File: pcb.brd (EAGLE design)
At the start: 88.9 x 70 mm, 70 parts, among them U1 MSP430F5172, U10 DCH010505S_EDJ_4, U11 ISO7420_D_8, U12 TS5A3357_DCU_8, U13 TS5A3357_DCU_8, U14 TLV2242_D_8, U2 ISO7221A_D_8, U3 MAX232E_D_16, U4 ISO7221A_D_8, U5 DCH010505S_EDJ_4, U6 REG101-3_DBV_5, U7 DCH010505S_EDJ_4, U8 TCA6416A_PW_24

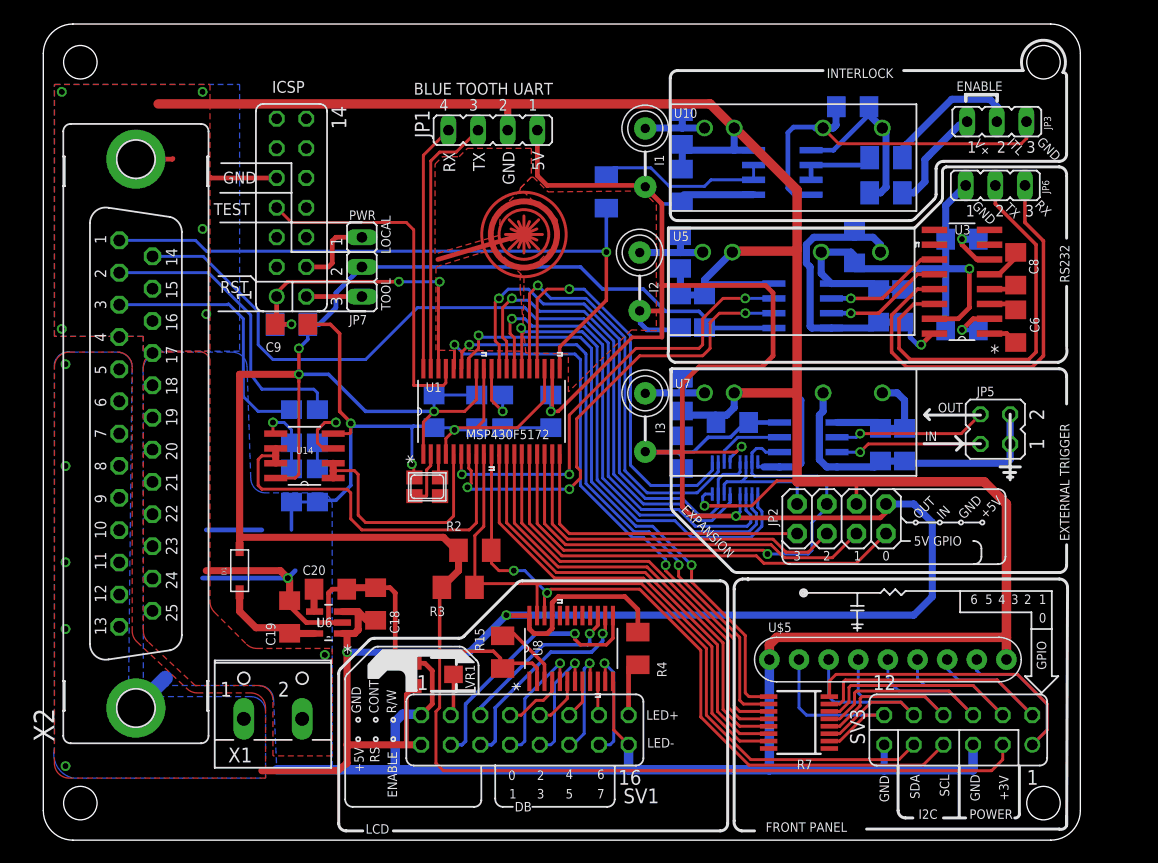
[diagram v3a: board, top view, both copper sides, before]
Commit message: Extensive Silkscreen update, LEDS
Added power, rx and tx LEDs
Updates silk screen documentation
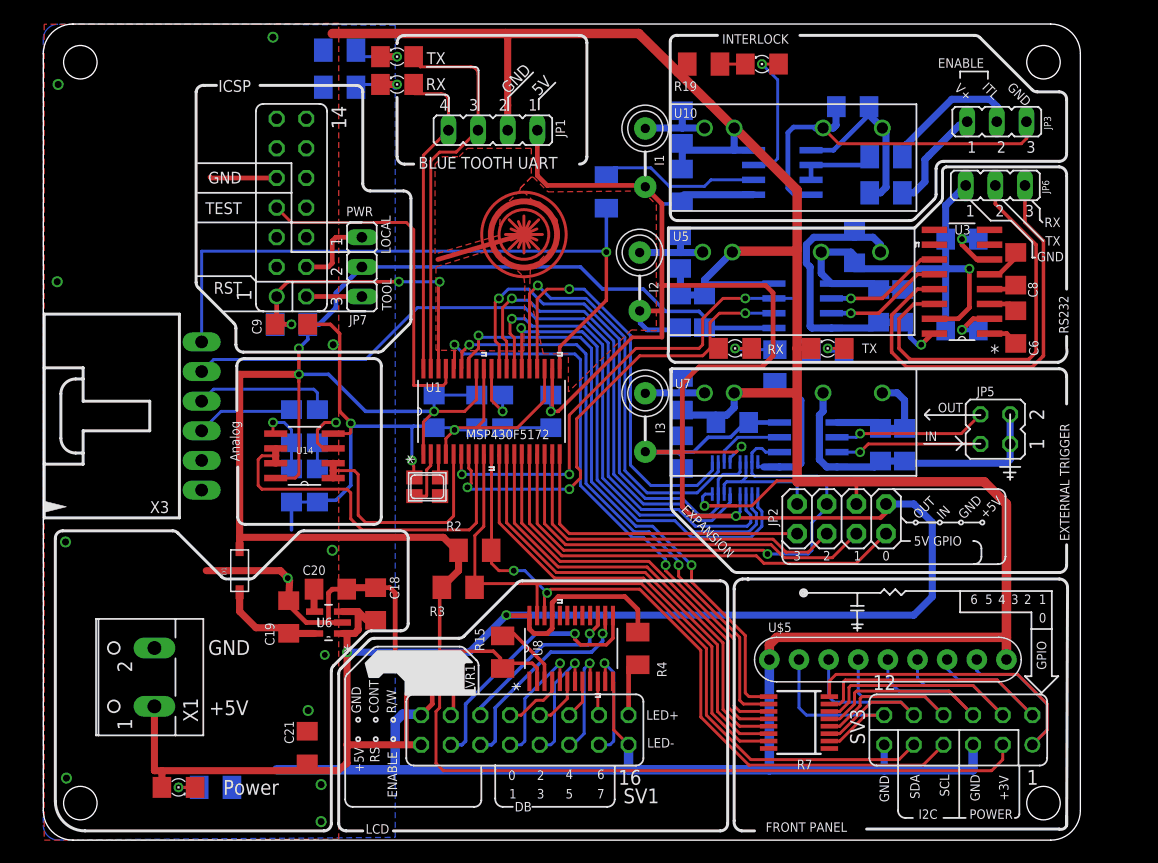
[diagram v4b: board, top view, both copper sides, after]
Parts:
- removed X2: (no value), con-subd:F25VP
- added C21: 10 uF, adafruit:C1206
- added LED1, LED2, LED3, LED4, LED5, LED6: (no value), led:1206
- added R12: 47k, adafruit:M1206
- added R13, R16, R17, R18, R19: 100k, adafruit:M1206
- added X3: C-GRID-06-70553, con-molex:70553-06
- R11: value 750k -> 100k
- U11: value ISO7420_D_8 -> ISO7420Fx
- moved X1 11.7 mm to (8.26, 14.0), turned to 90 degrees
- moved C16 0.08 mm to (54.8, 38.3)
- moved C19 0.08 mm to (21.0, 19.1)
- moved C29 0.08 mm to (54.8, 61.1)
- moved C6 0.08 mm to (83.3, 44.0)
- moved R5 0.08 mm to (72.2, 58.6)
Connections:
- new net N$25: LED1.C, R12.2
- new net N$26: LED2.C, R13.2
- new net N$29: LED3.C, R16.2
- new net N$30: LED6.C, R19.2
- new net N$31: LED5.C, R17.1
- new net N$32: LED6.A, U11.7
- new net N$33: LED4.A, R18.2
- net GND: now also C21.2, LED4.C, R12.1, R13.1, R16.1, R17.2, R19.1, X3.1, X3.2; no longer X2.17, X2.18, X2.19, X2.20, X2.21, X2.22, X2.23, X2.24, X2.25, X2.G1, X2.G2
- net LASER_CURRENT: now also X3.4; no longer X2.2
- net LASER_ILK: now also X3.6; no longer X2.1
- net LASER_ILK_HIGH: no longer U11.7
- net LASER_TEMPERATURE: now also X3.3; no longer X2.3
- net LASER_TTL: now also X3.5; no longer X2.14
- net RX1: now also LED5.A
- net RX2: now also LED3.A
- net TX1: now also R18.1
- net TX2: now also LED2.A
- net VCC_5V: now also C21.1, LED1.A; no longer X2.10, X2.11, X2.12, X2.13, X2.5, X2.6, X2.7, X2.8, X2.9
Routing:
- net GND: track 431.2 -> 408.3 mm, vias 11 -> 16
- net VCC_5V: track 258.9 -> 275.7 mm, vias 10 -> 5
- net LASER_TEMPERATURE: track 22.6 -> 8.45 mm
- net LASER_CURRENT: track 25.8 -> 11.9 mm
- net N$32: track 0.00 -> 12.4 mm, vias 0 -> 1
- net TX2: track 23.0 -> 34.4 mm
- net LASER_TTL: track 75.7 -> 66.5 mm
- net TX1: track 39.0 -> 45.9 mm
- net RX2: track 21.3 -> 27.9 mm
- net N$29: track 0.00 -> 5.95 mm, vias 0 -> 1
- net N$26: track 0.00 -> 5.50 mm, vias 0 -> 1
- net N$31: track 0.00 -> 4.88 mm, vias 0 -> 1
- net N$25: track 0.00 -> 3.20 mm, vias 0 -> 1
- net N$33: track 0.00 -> 2.92 mm, vias 0 -> 1
- net N$30: track 0.00 -> 2.18 mm
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- removed copper zone on layer 1, net VCC_5V
- removed copper zone on layer 16, net VCC_5V
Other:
- board text added: "Analog"
- board text added: "Current"
- board text added: "Interlock"
- board text added: "MCU"
- board text added: "Power"
- board text added: "Temperature"
- board text added: "Trigger"

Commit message: Silk updates
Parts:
- renumbered C1 to C8.5, C10 to C8.10, C11 to C8.9, C12 to C8.3, C13 to C8.2, C14 to C8.1, C15 to C6.3, C16 to C6.2, C17 to C6.1, C18 to C1.2, C19 to C1.4, C2 to C9.3, C20 to C1.3, C21 to C1.1, C29 to C9.2, C3 to C6.5, C30 to C9.1, C31 to C5.1, C32 to C5.2, C33 to C5.4, C34 to C5.3, C4 to C6.4, C5 to C8.4, C6 to C8.6, C7 to C8.8, C8 to C8.7, C9 to C7.1, I1 to L9.1, I2 to L8.1, I3 to L6.1, JP1 to H8.2, JP2 to H6.1, JP3 to H9.1, JP5 to H6.2, JP6 to H8.1, JP7 to H7.1, LED2 to LED8.3, LED3 to LED8.4, LED4 to LED8.1, LED5 to LED8.2, LED6 to LED9.1, Q2 to XTL, R1 to R4.1, R10 to R7.1, R11 to R9.1, R12 to R1.1, R13 to R8.3, R14 to R9.2, R15 to R2.1, R16 to R8.4, R17 to R8.2, R18 to R8.1, R19 to R9.4, R2 to R5.1, R3 to R5.2, R4 to R2.2, R5 to R9.3, R6 to R4.2, R7 to R3.1, R8 to R4.3, R9 to R4.4, SV1 to H2.1, SV3 to H3.1, U$5 to C3.1, U1 to MCU, U10 to U9.1, U11 to U9.2, U12 to U6.3, U13 to U6.4, U14 to U4.1, U2 to U6.2, U3 to U8.2, U4 to U8.3, U5 to U8.1, U6 to U1.1, U7 to U6.1, U8 to U2.1, X1 to EXT_POWER, X3 to LASER_COM
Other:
- board text added: "1.0"
- board text added: "1.1"
- board text added: "1.2"
- board text added: "1.3"
- board text added: "1.6"
- board text added: "2.0"
- board text added: "2.1"
- board text added: "2.2"
- board text added: "2013 Matthew Beals"
- board text added: "3.1"
- board text added: "3.2"
- board text added: "github.com/mjbeals/Laser_controller"

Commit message: Silk screen updates
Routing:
- net N$23: track 7.61 -> 0.00 mm
- removed copper zone on layer 1, net N$16
- removed copper zone on layer 1, net N$20
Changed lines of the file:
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@@
 <wire x1="1.031875" y1="3.33375" x2="1.031875" y2="25.87625" width="0.254" layer="121"/>
 <wire x1="1.031875" y1="25.87625" x2="1.666875" y2="26.51125" width="0.254" layer="121" curve="-90"/>
-<wire x1="30.63875" y1="26.51125" x2="31.27375" y2="25.87625" width="0.254" layer="121" curve="-90"/>
-<wire x1="31.27375" y1="25.87625" x2="31.27375" y2="18.57375" width="0.254" layer="121"/>
 <wire x1="31.27375" y1="18.57375" x2="30.63875" y2="17.93875" width="0.254" layer="121" curve="-90"/>
 <wire x1="30.63875" y1="17.93875" x2="28.12365" y2="17.93875" width="0.254" layer="121"/>
@@
 <wire x1="11.5366125" y1="26.3252625" x2="15.2921375" y2="22.5697375" width="0.254" layer="121"/>
 <wire x1="15.2921375" y1="22.5697375" x2="15.74115" y2="22.38375" width="0.254" layer="121" curve="45"/>
-<wire x1="30.559375" y1="26.51125" x2="22.329275" y2="26.51125" width="0.254" layer="121"/>
+<wire x1="31.0877625" y1="24.4747375" x2="29.2372375" y2="26.3252625" width="0.254" layer="121"/>
+<wire x1="29.2372375" y1="26.3252625" x2="28.788225" y2="26.51125" width="0.254" layer="121" curve="45"/>
+<wire x1="28.788225" y1="26.51125" x2="22.329275" y2="26.51125" width="0.254" layer="121"/>
 <wire x1="22.329275" y1="26.51125" x2="21.8802625" y2="26.3252625" width="0.254" layer="121" curve="45"/>
 <wire x1="21.8802625" y1="26.3252625" x2="18.1247375" y2="22.5697375" width="0.254" layer="121"/>
@@
 <wire x1="30.32125" y1="68.341875" x2="30.95625" y2="68.976875" width="0.254" layer="121" curve="-90"/>
 <wire x1="45.958125" y1="68.976875" x2="46.593125" y2="68.341875" width="0.254" layer="121" curve="-90"/>
-<wire x1="46.593125" y1="68.341875" x2="46.593125" y2="57.62625" width="0.254" layer="121"/>
-<wire x1="46.593125" y1="57.62625" x2="45.958125" y2="56.99125" width="0.254" layer="121" curve="-90"/>
-<wire x1="45.958125" y1="56.99125" x2="30.95625" y2="56.99125" width="0.254" layer="121"/>
+<wire x1="46.593125" y1="68.341875" x2="46.593125" y2="56.1975" width="0.254" layer="121"/>
+<wire x1="46.593125" y1="56.1975" x2="46.19625" y2="55.800625" width="0.254" layer="121" curve="-90"/>
+<wire x1="33.9725" y1="55.800625" x2="33.416875" y2="56.35625" width="0.254" layer="121" curve="-90"/>
+<wire x1="33.416875" y1="56.35625" x2="32.781875" y2="56.99125" width="0.254" layer="121" curve="90"/>
+<wire x1="32.781875" y1="56.99125" x2="30.95625" y2="56.99125" width="0.254" layer="121"/>
 <wire x1="30.32125" y1="63.65875" x2="30.32125" y2="57.62625" width="0.254" layer="121"/>
 <wire x1="39.84625" y1="62.5475" x2="39.84625" y2="63.65875" width="0.1524" layer="121"/>
@@
 <wire x1="47.704375" y1="68.976875" x2="52.54625" y2="68.976875" width="0.254" layer="121"/>
 <wire x1="52.54625" y1="68.976875" x2="53.18125" y2="68.341875" width="0.254" layer="121" curve="-90"/>
-<wire x1="53.18125" y1="27.860625" x2="52.54625" y2="27.225625" width="0.254" layer="121" curve="-90"/>
-<wire x1="52.54625" y1="27.225625" x2="47.704375" y2="27.225625" width="0.254" layer="121"/>
-<wire x1="47.704375" y1="27.225625" x2="47.069375" y2="27.94" width="0.254" layer="121" curve="-90"/>
+<wire x1="53.18125" y1="29.21" x2="52.3875" y2="28.575" width="0.254" layer="121" curve="-90"/>
+<wire x1="52.3875" y1="28.575" x2="47.545625" y2="28.575" width="0.254" layer="121"/>
+<wire x1="47.545625" y1="28.575" x2="47.069375" y2="29.21" width="0.254" layer="121" curve="-90"/>
 <wire x1="48.8677625" y1="42.0415125" x2="47.2553625" y2="40.4291125" width="0.254" layer="121"/>
 <wire x1="47.2553625" y1="40.4291125" x2="47.069375" y2="39.9801" width="0.254" layer="121" curve="45"/>
-<wire x1="47.069375" y1="39.9801" x2="47.069375" y2="27.94" width="0.254" layer="121"/>
+<wire x1="47.069375" y1="39.9801" x2="47.069375" y2="29.21" width="0.254" layer="121"/>
 <wire x1="53.18125" y1="68.341875" x2="53.18125" y2="62.309375" width="0.254" layer="121"/>
 <wire x1="53.18125" y1="59.610625" x2="53.18125" y2="39.6875" width="0.254" layer="121"/>
-<wire x1="53.18125" y1="36.909375" x2="53.18125" y2="27.860625" width="0.254" layer="121"/>
+<wire x1="53.18125" y1="36.909375" x2="53.18125" y2="29.21" width="0.254" layer="121"/>
 <wire x1="30.95625" y1="56.99125" x2="30.32125" y2="57.62625" width="0.254" layer="121" curve="-90"/>
-<wire x1="47.069375" y1="68.341875" x2="47.14875" y2="68.341875" width="0.254" layer="121"/>
-<wire x1="47.14875" y1="68.341875" x2="47.14875" y2="57.62625" width="0.254" layer="121"/>
-<wire x1="47.14875" y1="57.62625" x2="47.78375" y2="56.99125" width="0.254" layer="121" curve="90"/>
-<wire x1="47.78375" y1="56.99125" x2="48.41875" y2="56.99125" width="0.254" layer="121"/>
-<wire x1="48.41875" y1="56.99125" x2="49.05375" y2="56.35625" width="0.254" layer="121" curve="-90"/>
-<wire x1="49.05375" y1="56.35625" x2="49.05375" y2="42.490525" width="0.254" layer="121"/>
+<wire x1="47.069375" y1="68.341875" x2="47.069375" y2="68.2625" width="0.254" layer="121" curve="-90"/>
+<wire x1="47.069375" y1="68.2625" x2="47.069375" y2="56.276875" width="0.254" layer="121"/>
+<wire x1="47.069375" y1="56.276875" x2="47.863125" y2="55.800625" width="0.254" layer="121" curve="90"/>
+<wire x1="47.863125" y1="55.800625" x2="48.498125" y2="55.800625" width="0.254" layer="121"/>
+<wire x1="48.498125" y1="55.800625" x2="49.05375" y2="55.245" width="0.254" layer="121" curve="-90"/>
+<wire x1="49.05375" y1="55.245" x2="49.05375" y2="42.490525" width="0.254" layer="121"/>
 <wire x1="49.05375" y1="42.490525" x2="48.8677625" y2="42.0415125" width="0.254" layer="121" curve="-45"/>
+<wire x1="31.27375" y1="18.57375" x2="31.27375" y2="24.025725" width="0.254" layer="121"/>
+<wire x1="31.27375" y1="24.025725" x2="31.0877625" y2="24.4747375" width="0.254" layer="121" curve="45"/>
+<wire x1="33.9725" y1="55.800625" x2="38.57625" y2="55.800625" width="0.254" layer="121"/>
+<wire x1="46.116875" y1="55.800625" x2="43.815" y2="55.800625" width="0.254" layer="121"/>
+<wire x1="38.57625" y1="55.800625" x2="43.815" y2="55.800625" width="0.254" layer="121" curve="-68.17254"/>
 </plain>
 <attributes>
@@
 <wire x1="41.195625" y1="51.91125" x2="42.306875" y2="51.435" width="0.254" layer="1"/>
 </signal>
-<signal name="N$12">
-<polygon width="0.254" layer="1" isolate="0.254">
-<vertex x="39.0525" y="51.831875"/>
-<vertex x="33.575625" y="50.244375"/>
-<vertex x="33.575625" y="57.94375"/>
-<vertex x="34.210625" y="58.57875"/>
-<vertex x="35.639375" y="58.57875"/>
-<vertex x="36.35375" y="59.293125"/>
-<vertex x="41.830625" y="59.293125"/>
-<vertex x="41.830625" y="56.8325"/>
-<vertex x="40.878125" y="55.88"/>
-<vertex x="40.878125" y="55.72125"/>
-<vertex x="39.21125" y="54.054375"/>
-</polygon>
-</signal>
-<signal name="N$16">
-<polygon width="0.254" layer="1" isolate="0.254">
-<vertex x="33.655" y="49.133125"/>
-<vertex x="37.465" y="50.32375"/>
-<vertex x="38.89375" y="50.561875"/>
-<vertex x="41.195625" y="48.26"/>
-<vertex x="41.275" y="47.545625"/>
-<vertex x="41.195625" y="43.18"/>
-<vertex x="41.195625" y="41.91"/>
-<vertex x="33.655" y="41.989375"/>
-</polygon>
-</signal>
-<signal name="N$20">
-<polygon width="0.254" layer="1" isolate="0.254">
-<vertex x="41.830625" y="56.8325"/>
-<vertex x="41.989375" y="56.8325"/>
-<vertex x="43.259375" y="55.5625"/>
-<vertex x="49.05375" y="55.5625"/>
-<vertex x="49.05375" y="42.306875"/>
-<vertex x="45.005625" y="38.4175"/>
-<vertex x="45.005625" y="41.671875"/>
-<vertex x="42.8625" y="41.671875"/>
-<vertex x="41.671875" y="46.83125"/>
-<vertex x="41.75125" y="49.133125"/>
-<vertex x="41.989375" y="49.133125"/>
-<vertex x="44.053125" y="51.196875"/>
-<vertex x="44.053125" y="53.18125"/>
-<vertex x="42.545" y="54.689375"/>
-<vertex x="42.06875" y="54.689375"/>
-<vertex x="40.878125" y="55.88"/>
-</polygon>
-</signal>
-<signal name="N$23">
-<wire x1="33.81375" y1="49.768125" x2="41.11625" y2="51.91125" width="0.4064" layer="1"/>
-</signal>
 <signal name="N$25">
 <contactref element="LED1" pad="C"/>
@@
 <wire x1="63.017" y1="66.51625" x2="61.595" y2="66.51625" width="0.254" layer="1"/>
 </signal>
+<signal name="N$12">
+<polygon width="0.254" layer="1" isolate="0.254">
+<vertex x="33.17875" y="41.5925"/>
+<vertex x="44.846875" y="41.5925"/>
+<vertex x="44.846875" y="37.861875"/>
+<vertex x="45.323125" y="38.4175"/>
+<vertex x="48.8857" y="42.283271875" curve="42.662879"/>
+<vertex x="49.05375" y="42.7136"/>
+<vertex x="49.05375" y="55.483125" curve="90"/>
+<vertex x="48.41875" y="56.118125"/>
+<vertex x="43.259375" y="56.118125"/>
+<vertex x="42.38625" y="56.99125"/>
+<vertex x="42.38625" y="58.975625"/>
+<vertex x="34.051875" y="58.975625"/>
+<vertex x="33.17875" y="58.181875"/>
+</polygon>
+</signal>
 </signals>
